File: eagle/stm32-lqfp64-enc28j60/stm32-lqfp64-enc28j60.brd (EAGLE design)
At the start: 160 x 100 mm, 36 parts, among them IC2 LM1117IDTX-3.3, IC3 LP2950, X1 MINI-USB-UX60-MB-5ST

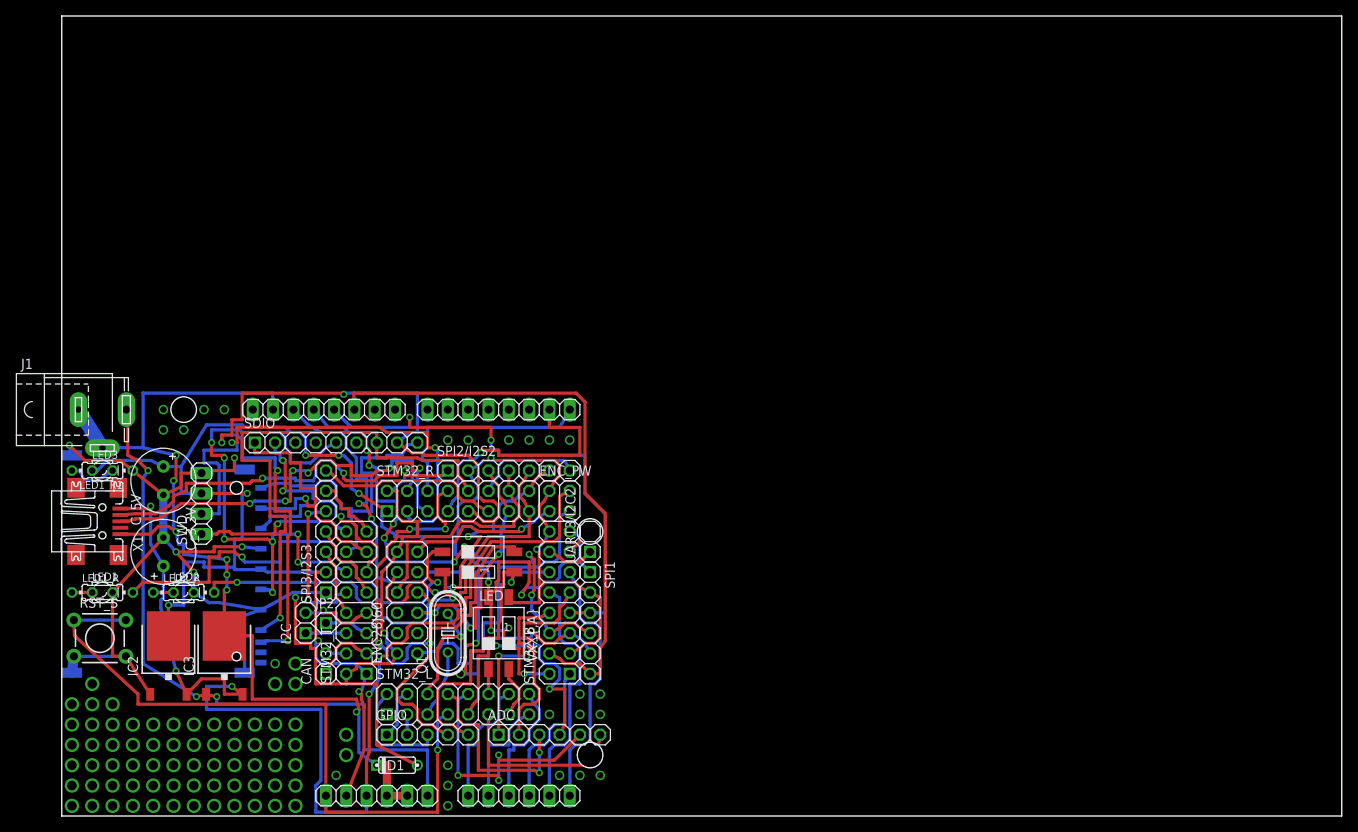
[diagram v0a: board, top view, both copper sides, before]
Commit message: Dimensions fixes
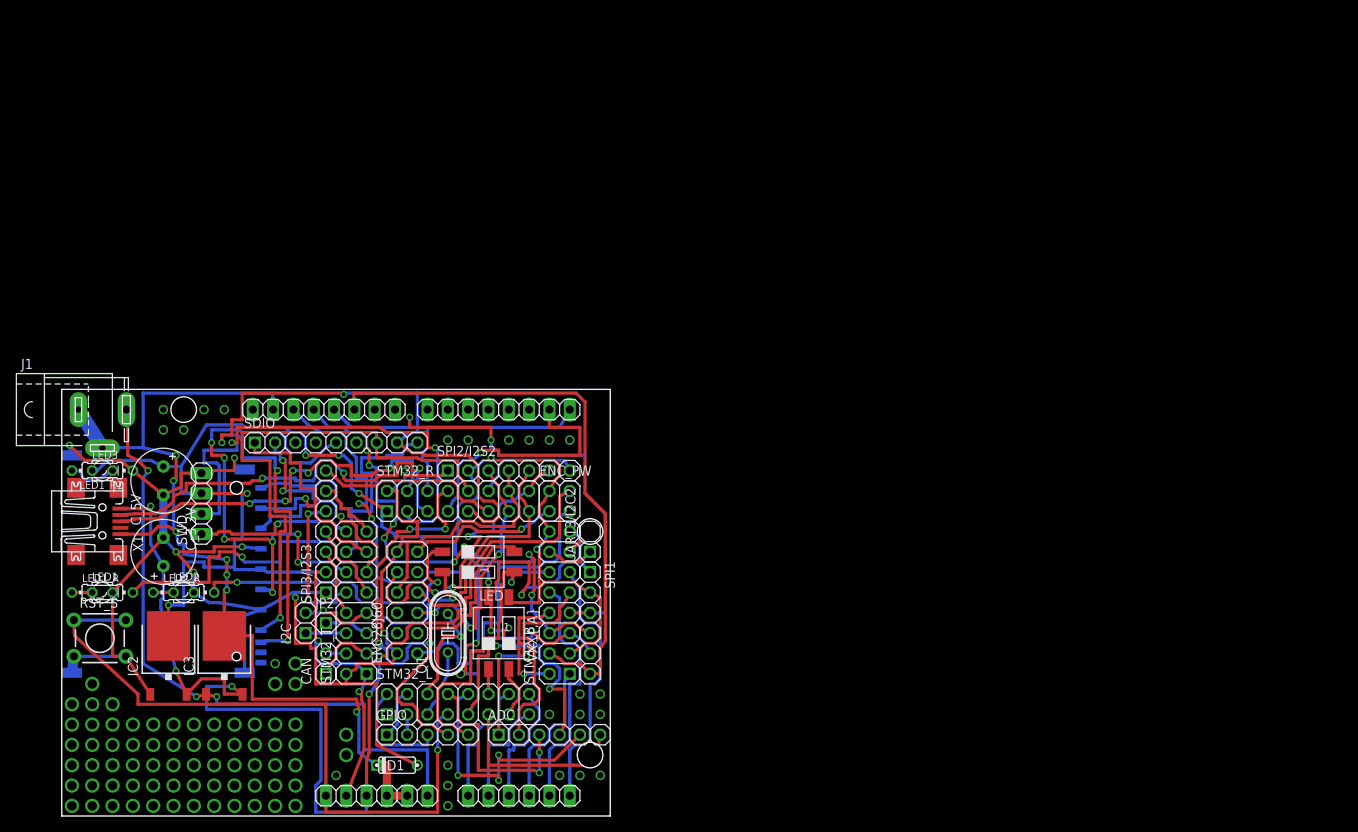
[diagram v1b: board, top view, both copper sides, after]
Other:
- board size 160 x 100 mm -> 68.6 x 53.3 mm
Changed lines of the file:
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@@
 <layer number="18" name="Vias" color="2" fill="1" visible="yes" active="yes"/>
 <layer number="19" name="Unrouted" color="6" fill="1" visible="yes" active="yes"/>
-<layer number="20" name="Dimension" color="15" fill="1" visible="yes" active="yes"/>
+<layer number="20" name="Dimension" color="15" fill="1" visible="no" active="yes"/>
 <layer number="21" name="tPlace" color="7" fill="1" visible="yes" active="yes"/>
 <layer number="22" name="bPlace" color="7" fill="1" visible="yes" active="yes"/>
@@
 <board>
 <plain>
-<wire x1="0" y1="0" x2="160" y2="0" width="0" layer="20"/>
-<wire x1="160" y1="0" x2="160" y2="100" width="0" layer="20"/>
-<wire x1="160" y1="100" x2="0" y2="100" width="0" layer="20"/>
-<wire x1="0" y1="100" x2="0" y2="0" width="0" layer="20"/>
+<wire x1="0" y1="0" x2="68.56" y2="0" width="0" layer="20"/>
+<wire x1="68.56" y1="0" x2="68.56" y2="53.3275" width="0" layer="20"/>
+<wire x1="68.56" y1="53.3275" x2="0" y2="53.3275" width="0" layer="20"/>
+<wire x1="0" y1="53.3275" x2="0" y2="0" width="0" layer="20"/>
 </plain>
 <attributes>
